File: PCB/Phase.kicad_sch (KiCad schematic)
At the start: 26 parts, among them Q1 SIR626LDP, Q2 SIR626LDP, U1 UCC27282, U6 INA180A3

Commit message: f
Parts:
- removed C2: 100p, symbol Device:C_Small
- removed C3: 1n, symbol Device:C_Small
- removed C4: 1u, symbol Device:C_Small
- removed R13: 0m5, symbol Device:R_Small
- removed R5: 8k2, symbol Device:R_Small
- removed R6, R7: 1k, symbol Device:R_Small
- removed U6: INA180A3, Package_TO_SOT_SMD:SOT-23-5, symbol Amplifier_Current:INA180A3
- Q1, Q2: value SIR626LDP -> TPHR8504PL
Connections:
- net GNDREF: now reaches Q2.3 (S)
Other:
- note added: "= 23 / 6.9 = 3.33nF"
- note added: "Qg = 23nC"
- note removed: "(25.5V * 1) / (8.2 + 1) = 2.77V"
- note removed: "50 * 0.0005 * 100 = 2.5V"
- note removed: "= 135 / 6.9 = 19.57nF"
- note removed: "ADC reference voltage = 2V9"
- note removed: "Gain = 50"
- note removed: "LPF BW = 159.24kHz"
- note removed: "Qg = 135nC"
- note removed: "Use kelvin connections to current sense resistors for best accuracy"
- moved on the sheet: C1, C18, C21, C24, C27, C30, C33, C5, D1, D2, Q1, Q2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

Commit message: f
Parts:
- removed Q1, Q2: TPHR8504PL, symbol Device:Q_NMOS_GDS
- added Q1, Q2: TPHR8504PL, Ariamelon-Package:SOP-8-Advance_5.0x6.0mm_P1.27mm, symbol Transistor_FET:BSC13DN30NSFD
- U5: renamed from U1; footprint (none) -> Ariamelon-Package:SOIC-8_3.9x4.9mm_P1.27mm
- renumbered C18 to C22, C21 to C23, C5 to C24, C1 to C25, C24 to C26, C30 to C28, C33 to C29, D1 to D5, D2 to D6, R30 to R21, R1 to R22, R2 to R24, R3 to R25, R4 to R26
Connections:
- net GNDREF: now also Q2.1 (S), Q2.2 (S), Q2.3 (S)
- net Phase_Out: now also Q1.1 (S), Q1.2 (S), Q1.3 (S), Q2.5 (D)
- net VCC: now also Q1.5 (D)
- net at R24.2, R26.2: now also Q2.4 (G)
- net at R22.2, R25.2: now also Q1.4 (G)

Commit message: d
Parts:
- removed C23, C25: 100n, symbol Device:C_Small
- removed C24: 1n, symbol Device:C_Small
- removed C28, C29: 4u7, symbol Device:C_Small
- removed D5, D6: 4148, symbol Device:D_Small
- removed R21: 2R2, symbol Device:R_Small
- removed R25, R26: 10, symbol Device:R_Small
- removed U5: UCC27282, Ariamelon-Package:SOIC-8_3.9x4.9mm_P1.27mm, symbol Ariamelon-IC:UCC27282
- added C6: 1n, Ariamelon-Device:C_0603_1608Metric, symbol Device:C_Small
- added C6: 1u, Ariamelon-Device:C_0603_1608Metric, symbol Device:C_Small
- added C9: 100n, Ariamelon-Device:C_0603_1608Metric, symbol Device:C_Small
- added D1, D4: 4148, Diode_SMD:D_SOD-123, symbol Device:D_Small
- added L1: L_Small, symbol Device:L_Small
- added R1, R10: 10, Ariamelon-Device:R_0603_1608Metric, symbol Device:R_Small
- added U1: UCC27282DRM, Ariamelon-Package:Texas_S-PVSON-N8-1EP_4x4mm_P0.8_EP2.5x3.4mm, symbol Ariamelon-IC:UCC27282DRM
- C1: renamed from C26; footprint (none) -> Ariamelon-Device:C_1206_3216Metric
- C10: renamed from C22; value 4u7 -> 1u; footprint (none) -> Ariamelon-Device:C_0603_1608Metric
- C5: renamed from C27; footprint (none) -> Ariamelon-Device:C_1206_3216Metric
- R2: renamed from R22; value 22R -> 22; footprint (none) -> Ariamelon-Device:R_0603_1608Metric
- R4: renamed from R24; value 22R -> 22; footprint (none) -> Ariamelon-Device:R_0603_1608Metric
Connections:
- net GND: now also C9.1, U1.7 (VSS), U1.9 (EP); no longer C1.1, C5.1
- net GNDREF: now also C1.1, C5.1
- net HI: now also U1.5 (HI)
- net LI: now also U1.6 (LI)
- net Phase_Out: now also C6.1, C6.1, U1.4 (HS)
- net at C10.2: now also C9.2, L1.2, U1.1 (VDD)
- net at R4.1: now also D4.1 (K), U1.8 (LO)
- net at Q2.4 (G), R4.2: now also R10.2
- net at Q1.4 (G), R2.2: now also R1.2
- net at R2.1: now also D1.1 (K), U1.3 (HO)
- new net: C6.2, C6.2, U1.2 (HB)
- new net: D4.2 (A), R10.1
- new net: D1.2 (A), R1.1
- new net +10V: L1.1
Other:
- note added: "= 10 * 49 = 490nF"
- note added: "Cb > 10 * Qg"
- note added: "Must size boot capacitor to account for skipped pulses and switching times!"
- note added: "Qg = 49nC @ 4.5V"
- note added: "Selected value = 1u"
- note removed: "= 12 - 1 - (4.4 - 0.3) = 6.9V"
- note removed: "= 23 / 6.9 = 3.33nF"
- note removed: "Added 1nF for HF filtering as per datasheet"
- note removed: "Cboot(min) = Qg / ΔVhb"
- note removed: "Must oversize boot capacitor to account for skipped pulses and switching times!"
- note removed: "Qg = 23nC"
- note removed: "Selected value = 100nF"
- note removed: "ΔVhb = Vdd - Vdh - (Vhbr(max) - Vhbh)"
- moved on the sheet: C1, C10, C5, Q1, Q2, R2, R4

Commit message: f
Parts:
- removed C9: 100n, Ariamelon-Device:C_0603_1608Metric, symbol Device:C_Small
- added C2: 10n, Ariamelon-Device:C_0603_1608Metric, symbol Device:C_Small
- C3: renamed from C6; value 1n -> 10n
- C5: renamed from C1; footprint Ariamelon-Device:C_1206_3216Metric -> Ariamelon-Device:C_0805_2012Metric
- C6: renamed from C5; footprint Ariamelon-Device:C_1206_3216Metric -> Ariamelon-Device:C_0805_2012Metric
- U1: footprint Ariamelon-Package:Texas_S-PVSON-N8-1EP_4x4mm_P0.8_EP2.5x3.4mm -> Ariamelon-Package:SOIC-8_3.9x4.9mm_P1.27mm
- renumbered C10 to C1, C6 to C4, D4 to D2, R2 to R1, R4 to R2, R1 to R3, R10 to R4
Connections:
- net GND: now also C2.2
- net at C1.2, L1.2, U1.1 (VDD): now also C2.1

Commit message: f
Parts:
- removed Q1, Q2: TPHR8504PL, Ariamelon-Package:SOP-8-Advance_5.0x6.0mm_P1.27mm, symbol Transistor_FET:BSC13DN30NSFD
- added Q1, Q2: Q_NMOS_GDS, Package_TO_SOT_SMD:TO-252-2, symbol Device:Q_NMOS_GDS
- added R5, R6: 100k, Ariamelon-Device:R_0603_1608Metric, symbol Device:R_Small
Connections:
- net GNDREF: now also Q2.3 (S), R6.2
- net Phase_Out: now also Q1.3 (S), Q2.2 (D), R5.2
- net VCC: now also Q1.2 (D)
- net at R2.2, R4.2: now also Q2.1 (G), R6.1
- net at R1.2, R3.2: now also Q1.1 (G), R5.1
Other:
- moved on the sheet: D2, R2, R4

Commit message: f
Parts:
- removed C3: 10n, Ariamelon-Device:C_0603_1608Metric, symbol Device:C_Small
- D1, D2: footprint Diode_SMD:D_SOD-123 -> Ariamelon-Device:D_SOD-323
- L1: footprint (none) -> Ariamelon-Device:L_0603_1608Metric
- Q1, Q2: footprint Package_TO_SOT_SMD:TO-252-2 -> Ariamelon-Package:TO-252-2
- R1, R2: value 22 -> 10
- R3, R4: value 10 -> 22
- U1: value UCC27282DRM -> UCC27211ADRM
- renumbered C4 to C3, C5 to C4, C6 to C5
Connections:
- net at D2.1 (K), U1.8 (LO): now also R4.1; no longer R2.1
- net at D2.2 (A): now also R2.1; no longer R4.1
- net at D1.1 (K), U1.3 (HO): now also R3.1; no longer R1.1
- net at D1.2 (A): now also R1.1; no longer R3.1
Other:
- moved on the sheet: C1, C2, C3, C4, C5, L1, Q1, Q2, R5, R6

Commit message: Completed initial prototype.
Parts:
- removed C2: 10n, Ariamelon-Device:C_0603_1608Metric, symbol Device:C_Small
- removed C4, C5: 4u7, Ariamelon-Device:C_0805_2012Metric, symbol Device:C_Small
- removed L1: L_Small, Ariamelon-Device:L_0603_1608Metric, symbol Device:L_Small
- added D3, D4: 15V, Diode_THT:D_DO-35_SOD27_P7.62mm_Horizontal, symbol Device:D_Zener_Small
- added D5, D6: 400x, Diode_THT:D_DO-35_SOD27_P7.62mm_Horizontal, symbol Device:D_Small
- added R1: 1, Resistor_THT:R_Axial_DIN0204_L3.6mm_D1.6mm_P7.62mm_Horizontal, symbol Device:R_Small
- C1: value 1u -> 10u; footprint Ariamelon-Device:C_0603_1608Metric -> Ariamelon-Device:CP_Radial_D5.0mm_P2.54mm; symbol Device:C_Small -> Device:C_Polarized_Small
- C2: renamed from C3; value 1u -> 680n; footprint Ariamelon-Device:C_0603_1608Metric -> Ariamelon-Device:C_Rect_L7.0mm_W4.5mm_P5.08mm
- D1, D2: footprint Ariamelon-Device:D_SOD-323 -> Diode_THT:D_DO-35_SOD27_P7.62mm_Horizontal
- Q1, Q2: value Q_NMOS_GDS -> P75NF75; footprint Ariamelon-Package:TO-252-2 -> Package_TO_SOT_THT:TO-220-3_Vertical
- R2: renamed from R3; footprint Ariamelon-Device:R_0603_1608Metric -> Resistor_THT:R_Axial_DIN0204_L3.6mm_D1.6mm_P7.62mm_Horizontal
- R3: renamed from R4; footprint Ariamelon-Device:R_0603_1608Metric -> Resistor_THT:R_Axial_DIN0204_L3.6mm_D1.6mm_P7.62mm_Horizontal
- R4: renamed from R1; footprint Ariamelon-Device:R_0603_1608Metric -> Resistor_THT:R_Axial_DIN0204_L3.6mm_D1.6mm_P7.62mm_Horizontal
- R5: renamed from R2; footprint Ariamelon-Device:R_0603_1608Metric -> Resistor_THT:R_Axial_DIN0204_L3.6mm_D1.6mm_P7.62mm_Horizontal
- R6: renamed from R5; footprint Ariamelon-Device:R_0603_1608Metric -> Resistor_THT:R_Axial_DIN0204_L3.6mm_D1.6mm_P7.62mm_Horizontal
- R7: renamed from R6; footprint Ariamelon-Device:R_0603_1608Metric -> Resistor_THT:R_Axial_DIN0204_L3.6mm_D1.6mm_P7.62mm_Horizontal
- U1: value UCC27211ADRM -> UCC27282; footprint Ariamelon-Package:SOIC-8_3.9x4.9mm_P1.27mm -> Package_DIP:DIP-8_W7.62mm_Socket
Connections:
- net GNDREF is gone; now on net GND: Q2.3 (S), R7.2
- net GND: now also C1.2, D4.2 (A), D6.2 (A); no longer C1.1
- net Phase_Out: now also D3.2 (A), D5.2 (A), D6.1 (K)
- net VCC: now also D5.1 (K)
- net at U1.1 (VDD): now also C1.1, R1.2; no longer C1.2
- net at Q1.1 (G), R2.2, R4.2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: now also D3.1 (K)
- net at Q2.1 (G), R3.2, R5.2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: now also D4.1 (K)
- new net +12V: R1.1
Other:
- note added: "-3dB point = 15.9kHz"
- note added: "FET gates discharge faster than they charge to avoid cross-conduction"
- note added: "No need for any special circuitry to prevent this"
- note added: "Selected value = 1u (increase if necessary)"
- note added: "UCC27282 has input interlock protection"
- note removed: "= 10 * 49 = 490nF"
- note removed: "Cb > 10 * Qg"
- note removed: "Cboot equations"
- note removed: "Qg = 49nC @ 4.5V"
- note removed: "Selected value = 1u"
- moved on the sheet: C2, D1, D2, Q1, Q2, R2, R3, R4, R5, R6, R7, U1

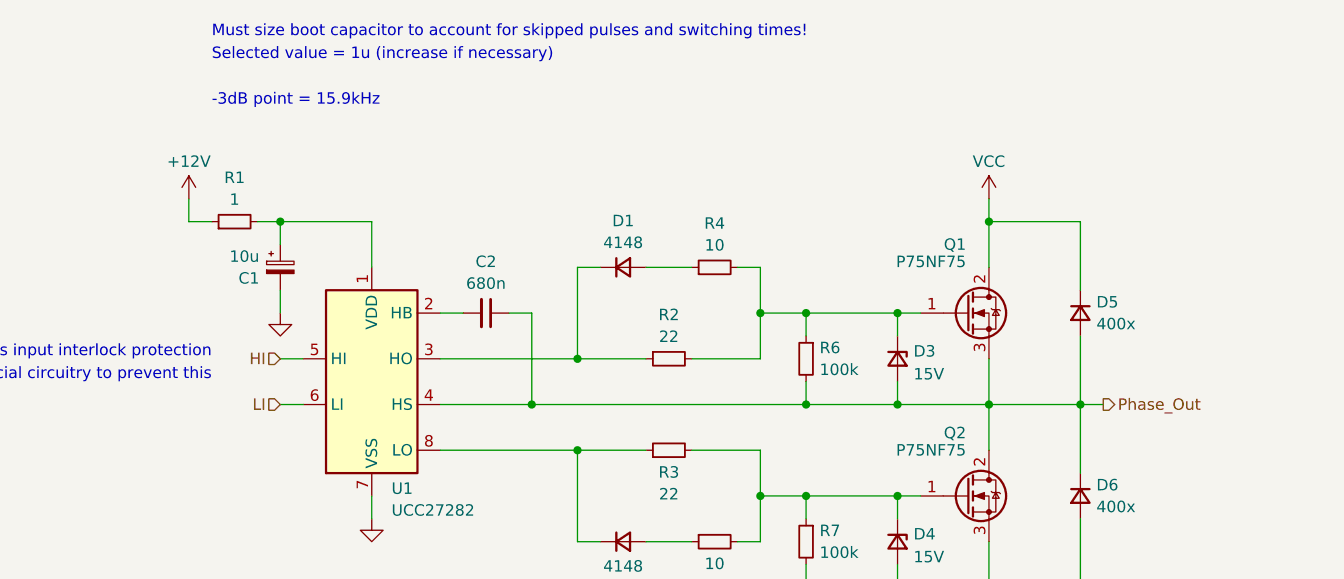
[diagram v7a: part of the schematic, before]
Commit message: Fixed pin assignment. Added tentative arduino code.
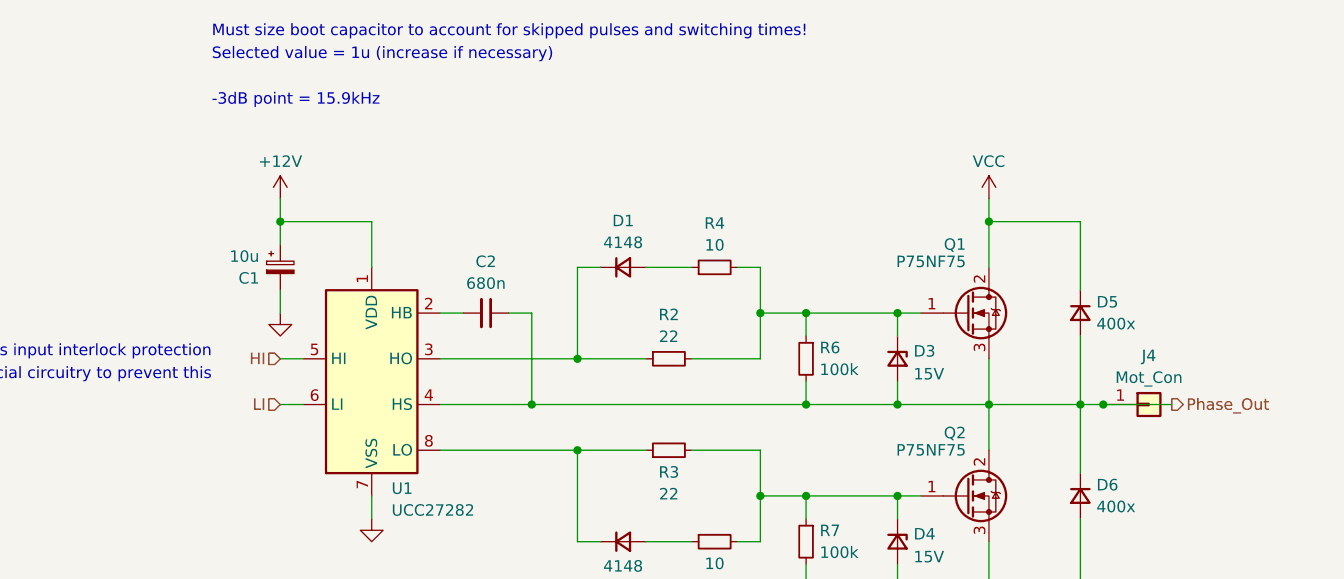
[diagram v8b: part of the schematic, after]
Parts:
- removed R1: 1, Resistor_THT:R_Axial_DIN0204_L3.6mm_D1.6mm_P7.62mm_Horizontal, symbol Device:R_Small
- added J4: Mot_Con, Ariamelon-HolePad:MountingHole_3.2mm_M3_Pad, symbol Connector_Generic:Conn_01x01
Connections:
- net +12V: now also C1.1, U1.1 (VDD)
- net Phase_Out: now also J4.1 (Pin_1)
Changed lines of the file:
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@@
   (junction (at 160.02 109.22) (diameter 0) (color 0 0 0 0)
   )
+  (junction (at 193.04 99.06) (diameter 0) (color 0 0 0 0)
+  )
   (junction (at 154.94 109.22) (diameter 0) (color 0 0 0 0)
   )
@@
     (stroke (width 0) (type default))
   )
+  (wire (pts (xy 193.04 99.06) (xy 200.66 99.06))
+    (stroke (width 0) (type default))
+  )
   (wire (pts (xy 134.62 83.82) (xy 137.16 83.82))
     (stroke (width 0) (type default))
@@
     (stroke (width 0) (type default))
   )
-  (wire (pts (xy 99.06 78.74) (xy 101.6 78.74))
-    (stroke (width 0) (type default))
-  )
   (wire (pts (xy 180.34 76.2) (xy 180.34 78.74))
     (stroke (width 0) (type default))
@@
     (stroke (width 0) (type default))
   )
-  (wire (pts (xy 91.44 78.74) (xy 93.98 78.74))
-    (stroke (width 0) (type default))
-  )
   (wire (pts (xy 119.38 88.9) (xy 121.92 88.9))
     (stroke (width 0) (type default))
@@
     (stroke (width 0) (type default))
   )
-  (wire (pts (xy 91.44 76.2) (xy 91.44 78.74))
+  (wire (pts (xy 101.6 76.2) (xy 101.6 78.74))
     (stroke (width 0) (type default))
   )
@@
     (effects (font (size 1.27 1.27)) (justify right))
   )
-  (hierarchical_label "Phase_Out" (shape output) (at 193.04 99.06 0) (fields_autoplaced)
+  (hierarchical_label "Phase_Out" (shape output) (at 200.66 99.06 0) (fields_autoplaced)
     (effects (font (size 1.27 1.27)) (justify left))
-  )
-  (symbol (lib_id "Device:R_Small") (at 96.52 78.74 90) (unit 1)
-    (in_bom yes) (on_board yes) (dnp no) (fields_autoplaced)
-    (property "Reference" "R1" (at 96.52 73.8591 90)
-      (effects (font (size 1.27 1.27)))
-    )
-    (property "Value" "1" (at 96.52 76.2833 90)
-      (effects (font (size 1.27 1.27)))
-    )
-    (property "Footprint" "Resistor_THT:R_Axial_DIN0204_L3.6mm_D1.6mm_P7.62mm_Horizontal" (at 96.52 78.74 0)
-      (effects (font (size 1.27 1.27)) hide)
-    )
-    (property "Datasheet" "~" (at 96.52 78.74 0)
-      (effects (font (size 1.27 1.27)) hide)
-    )
-    (property "Manufacturer no." "" (at 96.52 78.74 0)
-      (effects (font (size 1.27 1.27)) hide)
-    )
-    (pin "1")
-    (pin "2")
-    (instances
-      (project "BLDC-Controller"
-        (path "/3f98b8cc-f1be-42b2-9c23-c425b8147bc0/0df8a6da-2045-4c85-bcae-023f67988b04"
-          (reference "R1") (unit 1)
-        )
-        (path "/3f98b8cc-f1be-42b2-9c23-c425b8147bc0/359c123b-7597-4c48-9e5e-81f4f16bbab1"
-          (reference "R8") (unit 1)
-        )
-        (path "/3f98b8cc-f1be-42b2-9c23-c425b8147bc0/38eef514-6b7d-4a31-999e-913e758ed75e"
-          (reference "R15") (unit 1)
-        )
-      )
-    )
   )
   (symbol (lib_id "power:GND") (at 101.6 88.9 0) (unit 1)
@@
         (path "/3f98b8cc-f1be-42b2-9c23-c425b8147bc0/38eef514-6b7d-4a31-999e-913e758ed75e"
           (reference "R19") (unit 1)
+        )
+      )
+    )
+  )
+  (symbol (lib_id "Connector_Generic:Conn_01x01") (at 198.12 99.06 0) (unit 1)
+    (in_bom yes) (on_board yes) (dnp no) (fields_autoplaced)
+    (property "Reference" "J4" (at 198.12 93.6457 0)
+      (effects (font (size 1.27 1.27)))
+    )
+    (property "Value" "Mot_Con" (at 198.12 96.0699 0)
+      (effects (font (size 1.27 1.27)))
+    )
+    (property "Footprint" "Ariamelon-HolePad:MountingHole_3.2mm_M3_Pad" (at 198.12 99.06 0)
+      (effects (font (size 1.27 1.27)) hide)
+    )
+    (property "Datasheet" "~" (at 198.12 99.06 0)
+      (effects (font (size 1.27 1.27)) hide)
+    )
+    (pin "1")
+    (instances
+      (project "BLDC-Controller"
+        (path "/3f98b8cc-f1be-42b2-9c23-c425b8147bc0/0df8a6da-2045-4c85-bcae-023f67988b04"
+          (reference "J4") (unit 1)
+        )
+        (path "/3f98b8cc-f1be-42b2-9c23-c425b8147bc0/359c123b-7597-4c48-9e5e-81f4f16bbab1"
+          (reference "J5") (unit 1)
+        )
+        (path "/3f98b8cc-f1be-42b2-9c23-c425b8147bc0/38eef514-6b7d-4a31-999e-913e758ed75e"
+          (reference "J6") (unit 1)
         )
       )
@@
     )
   )
-  (symbol (lib_id "power:+12V") (at 91.44 76.2 0) (unit 1)
-    (in_bom yes) (on_board yes) (dnp no) (fields_autoplaced)
-    (property "Reference" "#PWR017" (at 91.44 80.01 0)
-      (effects (font (size 1.27 1.27)) hide)
-    )
-    (property "Value" "+12V" (at 91.44 72.0669 0)
-      (effects (font (size 1.27 1.27)))
-    )
-    (property "Footprint" "" (at 91.44 76.2 0)
-      (effects (font (size 1.27 1.27)) hide)
-    )
-    (property "Datasheet" "" (at 91.44 76.2 0)
-      (effects (font (size 1.27 1.27)) hide)
-    )
-    (pin "1")
-    (instances
-      (project "BLDC-Controller"
-        (path "/3f98b8cc-f1be-42b2-9c23-c425b8147bc0/5281a03e-d6ab-4142-84eb-776fec16e050"
-          (reference "#PWR017") (unit 1)
-        )
+  (symbol (lib_id "power:+12V") (at 101.6 76.2 0) (unit 1)
+    (in_bom yes) (on_board yes) (dnp no) (fields_autoplaced)
+    (property "Reference" "#PWR01" (at 101.6 80.01 0)
+      (effects (font (size 1.27 1.27)) hide)
+    )
+    (property "Value" "+12V" (at 101.6 72.0669 0)
+      (effects (font (size 1.27 1.27)))
+    )
+    (property "Footprint" "" (at 101.6 76.2 0)
+      (effects (font (size 1.27 1.27)) hide)
+    )
+    (property "Datasheet" "" (at 101.6 76.2 0)
+      (effects (font (size 1.27 1.27)) hide)
+    )
+    (pin "1")
+    (instances
+      (project "BLDC-Controller"
         (path "/3f98b8cc-f1be-42b2-9c23-c425b8147bc0/0df8a6da-2045-4c85-bcae-023f67988b04"
           (reference "#PWR01") (unit 1)
